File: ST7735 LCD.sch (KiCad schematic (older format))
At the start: 1 part, among them J30 LCD

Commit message: Change the LCD power to 5V, keep the 3.3V only for the backlight LED.
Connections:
- net labels added: VCC
- net labels removed: 3.3V
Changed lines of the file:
@@
 ~RESET
 Text HLabel 4100 1850 2    50   Input ~ 0
-3.3V
+VCC
 Text HLabel 4100 1950 2    50   Input ~ 0
 LED+

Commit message: Position heater filter capacitors closer to the power bus.
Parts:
- J30: footprint Connector_PinHeader_2.54mm:PinHeader_2x05_P2.54mm_Vertical -> Connector_IDC:IDC-Header_2x05_P2.54mm_Vertical
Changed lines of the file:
@@
 F 0 "J30" H 3750 2467 50  0000 C CNN
 F 1 "LCD" H 3750 2376 50  0000 C CNN
-F 2 "Connector_PinHeader_2.54mm:PinHeader_2x05_P2.54mm_Vertical" H 3700 2050 50  0001 C CNN
+F 2 "Connector_IDC:IDC-Header_2x05_P2.54mm_Vertical" H 3700 2050 50  0001 C CNN
 F 3 "~" H 3700 2050 50  0001 C CNN
 	1    3700 2050

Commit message: Update annotations.
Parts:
- removed J30: LCD, Connector_IDC:IDC-Header_2x05_P2.54mm_Vertical, symbol Connector_Generic:Conn_02x05_Odd_Even
- added J30: LCD, Connector_IDC:IDC-Header_2x06_P2.54mm_Vertical, symbol Connector_Generic:Conn_02x06_Odd_Even
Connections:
- net labels added: BTN_IN, ENC_A, ENC_B
- wire segments 12 -> 13
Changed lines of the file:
@@
 EESchema Schematic File Version 4
 LIBS:PrntrBoardV1-cache
-EELAYER 26 0
+EELAYER 29 0
 EELAYER END
 $Descr A4 11693 8268
@@
 L power:GND #PWR090
 U 1 1 5AFA6291
-P 4100 2350
-F 0 "#PWR090" H 4100 2100 50  0001 C CNN
-F 1 "GND" H 4105 2177 50  0000 C CNN
-F 2 "" H 4100 2350 50  0001 C CNN
-F 3 "" H 4100 2350 50  0001 C CNN
-	1    4100 2350
+P 3450 2400
+F 0 "#PWR090" H 3450 2150 50  0001 C CNN
+F 1 "GND" H 3455 2227 50  0000 C CNN
+F 2 "" H 3450 2400 50  0001 C CNN
+F 3 "" H 3450 2400 50  0001 C CNN
+	1    3450 2400
 	1    0    0    -1
 $EndComp
-Wire Wire Line
-	4100 2150 4000 2150
 Wire Wire Line
 	4100 2050 4000 2050
@@
 Text HLabel 3450 2250 0    50   Input ~ 0
 ~CS
+Wire Wire Line
+	3450 2250 3500 2250
+Text HLabel 4100 2150 2    50   Input ~ 0
+BTN_IN
+Wire Wire Line
+	4100 2150 4000 2150
 $Comp
-L Connector_Generic:Conn_02x05_Odd_Even J30
-U 1 1 5B08E113
+L Connector_Generic:Conn_02x06_Odd_Even J30
+U 1 1 5B6CF880
 P 3700 2050
 F 0 "J30" H 3750 2467 50  0000 C CNN
 F 1 "LCD" H 3750 2376 50  0000 C CNN
-F 2 "Connector_IDC:IDC-Header_2x05_P2.54mm_Vertical" H 3700 2050 50  0001 C CNN
+F 2 "Connector_IDC:IDC-Header_2x06_P2.54mm_Vertical" H 3700 2050 50  0001 C CNN
 F 3 "~" H 3700 2050 50  0001 C CNN
 	1    3700 2050
@@
 $EndComp
 Wire Wire Line
-	3450 2250 3500 2250
+	3500 2350 3450 2350
 Wire Wire Line
-	4000 2250 4100 2250
+	3450 2350 3450 2400
+Text HLabel 4100 2250 2    50   Input ~ 0
+ENC_A
+Text HLabel 4100 2350 2    50   Input ~ 0
+ENC_B
 Wire Wire Line
-	4100 2250 4100 2350
+	4100 2250 4000 2250
 Wire Wire Line
-	4100 2150 4100 2250
-Connection ~ 4100 2250
+	4100 2350 4000 2350
 $EndSCHEMATC

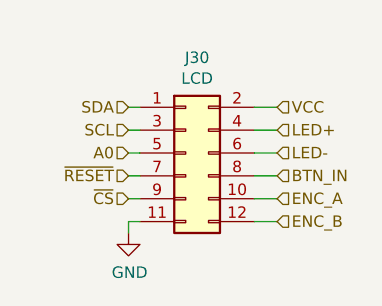
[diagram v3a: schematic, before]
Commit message: Reset schematics for tmc2660. Clean the board layout.
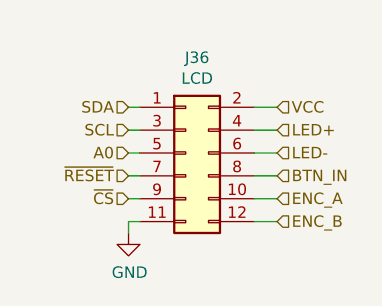
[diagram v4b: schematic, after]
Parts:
- renumbered J30 to J36
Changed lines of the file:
@@
 LED-
 $Comp
-L power:GND #PWR090
+L power:GND #PWR086
 U 1 1 5AFA6291
 P 3450 2400
-F 0 "#PWR090" H 3450 2150 50  0001 C CNN
+F 0 "#PWR086" H 3450 2150 50  0001 C CNN
 F 1 "GND" H 3455 2227 50  0000 C CNN
 F 2 "" H 3450 2400 50  0001 C CNN
@@
 	4100 2150 4000 2150
 $Comp
-L Connector_Generic:Conn_02x06_Odd_Even J30
+L Connector_Generic:Conn_02x06_Odd_Even J36
 U 1 1 5B6CF880
 P 3700 2050
-F 0 "J30" H 3750 2467 50  0000 C CNN
+F 0 "J36" H 3750 2467 50  0000 C CNN
 F 1 "LCD" H 3750 2376 50  0000 C CNN
 F 2 "Connector_IDC:IDC-Header_2x06_P2.54mm_Vertical" H 3700 2050 50  0001 C CNN
